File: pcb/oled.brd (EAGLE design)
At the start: 26.2 x 26.2 mm, 22 parts, among them U1 UG-2828GDEDF11, U3 FAN5331SX

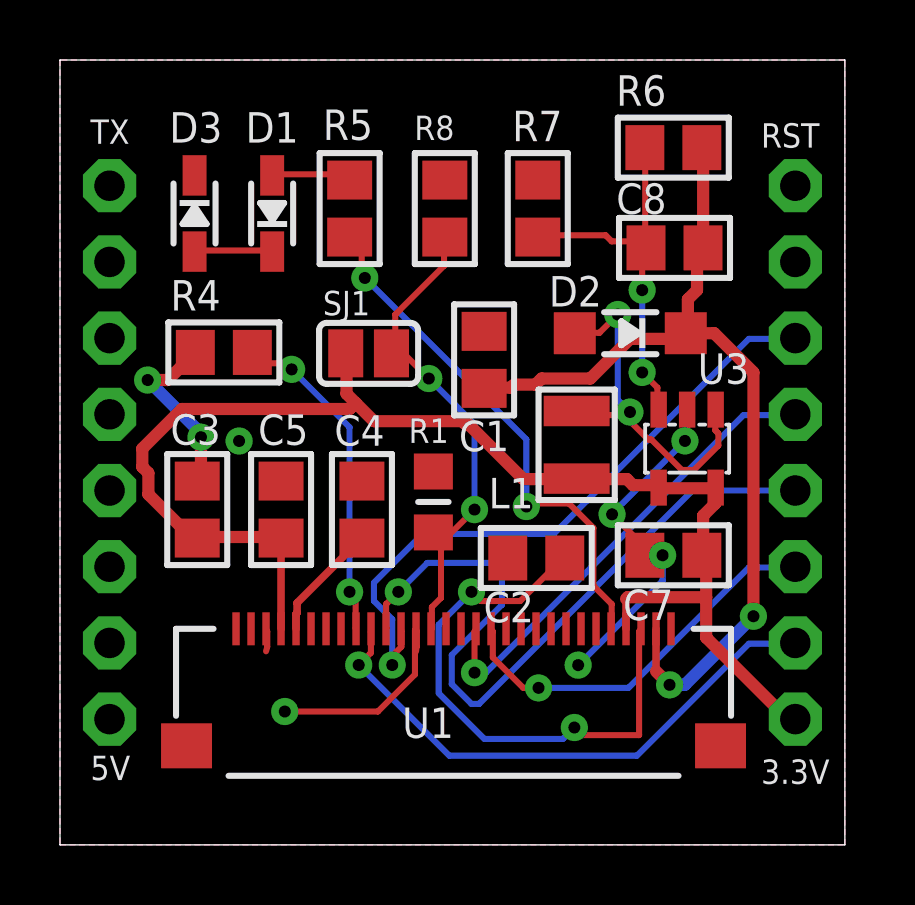
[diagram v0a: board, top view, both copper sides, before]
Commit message: USB board schematic V2 done
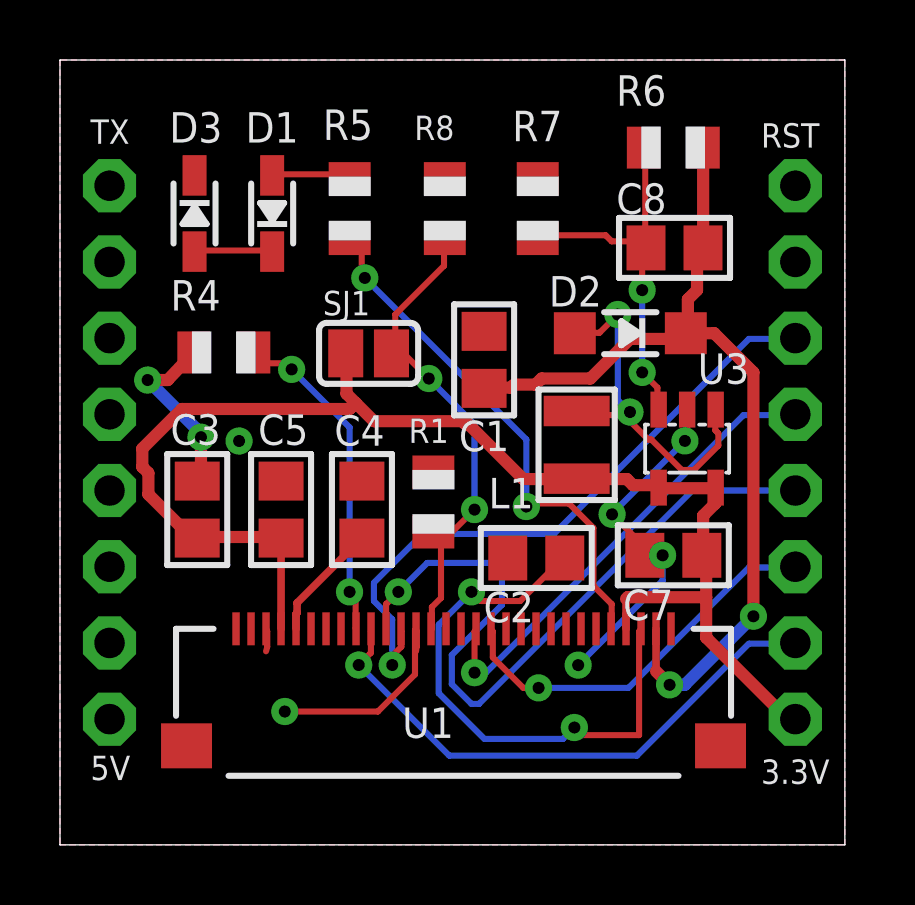
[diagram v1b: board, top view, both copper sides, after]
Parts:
- R1: device microbuilder:_0805MP -> adafruit:R0805
- R4, R5, R6, R7, R8: device microbuilder:0805 -> adafruit:R0805
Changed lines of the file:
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@@
 </autorouter>
 <elements>
-<element name="R4" library="microbuilder" package="0805" value="600K" x="5.461" y="16.414" smashed="yes">
+<element name="R4" library="adafruit" library_urn="urn:adsk.eagle:library:420" package="R0805" package3d_urn="urn:adsk.eagle:package:6240566/1" value="600K" x="5.461" y="16.414" smashed="yes">
 <attribute name="NAME" x="3.683" y="17.811" size="1.016" layer="25"/>
 <attribute name="VALUE" x="3.175" y="16.352" size="1.016" layer="27" rot="R180"/>
@@
 <attribute name="VALUE" x="4.194" y="8.763" size="1.016" layer="27" rot="R270"/>
 </element>
-<element name="R5" library="microbuilder" package="0805" value="50" x="9.655" y="21.209" smashed="yes" rot="R270">
+<element name="R5" library="adafruit" library_urn="urn:adsk.eagle:library:420" package="R0805" package3d_urn="urn:adsk.eagle:package:6240566/1" value="50" x="9.655" y="21.209" smashed="yes" rot="R270">
 <attribute name="NAME" x="8.763" y="23.498" size="1.016" layer="25"/>
 <attribute name="VALUE" x="9.274" y="17.907" size="1.016" layer="27" rot="R270"/>
@@
 <attribute name="NAME" x="16.296" y="17.944" size="1.016" layer="25"/>
 </element>
-<element name="R6" library="microbuilder" package="0805" value="100K" x="20.444" y="23.241" smashed="yes">
+<element name="R6" library="adafruit" library_urn="urn:adsk.eagle:library:420" package="R0805" package3d_urn="urn:adsk.eagle:package:6240566/1" value="100K" x="20.444" y="23.241" smashed="yes">
 <attribute name="NAME" x="18.539" y="24.638" size="1.016" layer="25"/>
 <attribute name="VALUE" x="18.793" y="21.209" size="1.016" layer="27"/>
 </element>
-<element name="R7" library="microbuilder" package="0805" value="10K" x="15.925" y="21.209" smashed="yes" rot="R270">
+<element name="R7" library="adafruit" library_urn="urn:adsk.eagle:library:420" package="R0805" package3d_urn="urn:adsk.eagle:package:6240566/1" value="10K" x="15.925" y="21.209" smashed="yes" rot="R270">
 <attribute name="NAME" x="15.076" y="23.455" size="1.016" layer="25"/>
 <attribute name="VALUE" x="17.693" y="19.775" size="1.016" layer="27" rot="R90"/>
@@
 <attribute name="NAME" x="3.646" y="23.408" size="1.016" layer="25"/>
 </element>
-<element name="R8" library="microbuilder" package="0805" value="10K" x="12.827" y="21.209" smashed="yes" rot="R270">
+<element name="R8" library="adafruit" library_urn="urn:adsk.eagle:library:420" package="R0805" package3d_urn="urn:adsk.eagle:package:6240566/1" value="10K" x="12.827" y="21.209" smashed="yes" rot="R270">
 <attribute name="NAME" x="11.811" y="23.495" size="0.8128" layer="25" ratio="18"/>
 <attribute name="VALUE" x="12.065" y="19.177" size="0.4064" layer="27" ratio="10" rot="R270"/>
@@
 <attribute name="VALUE" x="9.8869" y="16.383" size="0.02" layer="27" rot="R180"/>
 </element>
-<element name="R1" library="microbuilder" package="_0805MP" value="10K" x="12.446" y="11.43" smashed="yes" rot="R270">
+<element name="R1" library="adafruit" library_urn="urn:adsk.eagle:library:420" package="R0805" package3d_urn="urn:adsk.eagle:package:6240566/1" value="10K" x="12.446" y="11.43" smashed="yes" rot="R270">
 <attribute name="NAME" x="11.6205" y="13.3985" size="0.8128" layer="25" ratio="18"/>
 <attribute name="VALUE" x="11.176" y="13.0175" size="0.4064" layer="27" ratio="10" rot="R270"/>
@@
 <wire x1="12.7" y1="8.2296" x2="12.3952" y2="7.9248" width="0.2032" layer="1"/>
 <wire x1="12.7" y1="10.16" x2="12.7" y2="8.2296" width="0.2032" layer="1"/>
-<wire x1="12.446" y1="10.414" x2="12.7" y2="10.16" width="0.2032" layer="1"/>
+<wire x1="12.446" y1="10.43" x2="12.7" y2="10.16" width="0.2032" layer="1"/>
 <wire x1="12.3952" y1="7.2136" x2="12.368" y2="7.202" width="0.2032" layer="1"/>
 <wire x1="12.8016" y1="19.304" x2="12.8016" y2="20.2184" width="0.2032" layer="1"/>
@@
 <wire x1="11.176" y1="16.6624" x2="11.176" y2="17.6784" width="0.2032" layer="1"/>
 <wire x1="11.0744" y1="16.4592" x2="11.176" y2="16.5608" width="0.2032" layer="1"/>
-<wire x1="12.8016" y1="20.2184" x2="12.827" y2="20.259" width="0.2032" layer="1"/>
+<wire x1="12.8016" y1="20.2184" x2="12.827" y2="20.209" width="0.2032" layer="1"/>
 <wire x1="11.0744" y1="16.4592" x2="11.049" y2="16.383" width="0.2032" layer="1"/>
 <wire x1="12.9032" y1="10.2616" x2="12.7" y2="10.2616" width="0.2032" layer="1"/>
@@
 <wire x1="12.2936" y1="15.5448" x2="13.8176" y2="14.0208" width="0.2032" layer="16"/>
 <wire x1="11.176" y1="16.6624" x2="12.2936" y2="15.5448" width="0.2032" layer="1"/>
-<wire x1="12.7" y1="10.2616" x2="12.446" y2="10.414" width="0.2032" layer="1"/>
+<wire x1="12.7" y1="10.2616" x2="12.446" y2="10.43" width="0.2032" layer="1"/>
 <wire x1="11.176" y1="16.6624" x2="11.049" y2="16.383" width="0.2032" layer="1"/>
 <via x="13.8176" y="11.176" extent="1-16" drill="0.4"/>
@@
 <wire x1="11.8872" y1="7.112" x2="11.868" y2="7.202" width="0.2032" layer="1"/>
 <wire x1="11.8872" y1="6.604" x2="11.86798125" y2="6.452246875" width="0.2032" layer="1"/>
-<wire x1="4.511" y1="16.414" x2="3.591" y2="15.494" width="0.4064" layer="1"/>
+<wire x1="4.461" y1="16.414" x2="3.591" y2="15.494" width="0.4064" layer="1"/>
 <wire x1="3.591" y1="15.494" x2="2.921" y2="15.494" width="0.4064" layer="1"/>
 <via x="2.921" y="15.494" extent="1-16" drill="0.4"/>
@@
 <wire x1="20.0868" y1="8.806" x2="17.272" y2="5.9912" width="0.2032" layer="16"/>
 <via x="17.272" y="5.9912" extent="1-16" drill="0.4"/>
+<wire x1="12.827" y1="22.209" x2="15.925" y2="22.209" width="0" layer="19" extent="1-1"/>
+<wire x1="14.137" y1="17.116" x2="12.827" y2="22.209" width="0" layer="19" extent="1-1"/>
+<wire x1="12.446" y1="12.43" x2="14.137" y2="17.116" width="0" layer="19" extent="1-1"/>
+<wire x1="10.064" y1="12.126" x2="12.446" y2="12.43" width="0" layer="19" extent="1-1"/>
+<wire x1="7.369" y1="12.126" x2="10.064" y2="12.126" width="0" layer="19" extent="1-1"/>
+<wire x1="5.969" y1="13.462" x2="7.369" y2="12.126" width="0" layer="19" extent="1-1"/>
+<wire x1="4.699" y1="13.589" x2="5.969" y2="13.462" width="0" layer="19" extent="1-1"/>
+<wire x1="14.925" y1="9.562" x2="12.446" y2="12.43" width="0" layer="19" extent="1-1"/>
+<wire x1="18.4023" y1="11.01720625" x2="14.925" y2="9.562" width="0" layer="19" extent="1-1"/>
+<wire x1="20.368" y1="7.202" x2="20.0868" y2="9.652" width="0" layer="19" extent="1-1"/>
+<wire x1="11.868" y1="7.202" x2="14.925" y2="9.562" width="0" layer="19" extent="1-1"/>
+<wire x1="6.86798125" y1="6.45225" x2="7.493" y2="4.445" width="0" layer="19" extent="1-1"/>
+<wire x1="5.868" y1="7.202" x2="6.868" y2="7.202" width="0" layer="19" extent="1-1"/>
+<wire x1="1.651" y1="6.731" x2="5.868" y2="7.202" width="0" layer="19" extent="1-1"/>
+<wire x1="4.485" y1="22.315" x2="4.461" y2="16.414" width="0" layer="19" extent="1-1"/>
 </signal>
 <signal name="IREF">
@@
 <wire x1="6.5024" y1="16.3576" x2="6.8072" y2="16.0528" width="0.2032" layer="1"/>
 <wire x1="9.8552" y1="7.2136" x2="9.868" y2="7.202" width="0.2032" layer="1"/>
-<wire x1="6.5024" y1="16.3576" x2="6.411" y2="16.414" width="0.2032" layer="1"/>
+<wire x1="6.5024" y1="16.3576" x2="6.461" y2="16.414" width="0.2032" layer="1"/>
 <via x="9.652" y="8.4328" extent="1-16" drill="0.4"/>
 <via x="7.7216" y="15.8496" extent="1-16" drill="0.4"/>
@@
 <wire x1="9.7536" y1="20.2184" x2="10.0584" y2="19.9136" width="0.2032" layer="1"/>
 <wire x1="18.3896" y1="7.2136" x2="18.368" y2="7.202" width="0.2032" layer="1"/>
-<wire x1="9.7536" y1="20.2184" x2="9.655" y2="20.259" width="0.2032" layer="1"/>
+<wire x1="9.7536" y1="20.2184" x2="9.655" y2="20.209" width="0.2032" layer="1"/>
 <via x="15.5448" y="11.2776" extent="1-16" drill="0.4"/>
 <via x="10.16" y="18.8976" extent="1-16" drill="0.4"/>
@@
 <wire x1="9.652" y1="22.2504" x2="9.5504" y2="22.352" width="0.2032" layer="1"/>
 <wire x1="7.112" y1="22.352" x2="7.072" y2="22.315" width="0.2032" layer="1"/>
-<wire x1="9.652" y1="22.2504" x2="9.655" y2="22.159" width="0.2032" layer="1"/>
+<wire x1="9.652" y1="22.2504" x2="9.655" y2="22.209" width="0.2032" layer="1"/>
 </signal>
 <signal name="13V" class="1">
@@
 <wire x1="20.828" y1="16.8656" x2="20.86" y2="17.055" width="0.4064" layer="1"/>
 <wire x1="21.4376" y1="20.0152" x2="21.4376" y2="23.1648" width="0.4064" layer="1"/>
-<wire x1="21.4376" y1="23.1648" x2="21.394" y2="23.241" width="0.4064" layer="1"/>
+<wire x1="21.4376" y1="23.1648" x2="21.444" y2="23.241" width="0.4064" layer="1"/>
 <wire x1="21.4376" y1="20.0152" x2="21.434" y2="19.899" width="0.4064" layer="1"/>
 <wire x1="20.86" y1="17.055" x2="21.807" y2="17.055" width="0.4064" layer="1"/>
@@
 <wire x1="19.1008" y1="20.1168" x2="18.3896" y2="20.1168" width="0.2032" layer="1"/>
 <wire x1="19.4056" y1="19.812" x2="19.1008" y2="20.1168" width="0.2032" layer="1"/>
-<wire x1="15.9512" y1="20.32" x2="15.925" y2="20.259" width="0.2032" layer="1"/>
+<wire x1="15.9512" y1="20.32" x2="15.925" y2="20.209" width="0.2032" layer="1"/>
 <wire x1="19.4056" y1="19.812" x2="19.534" y2="19.899" width="0.2032" layer="1"/>
 <wire x1="19.5072" y1="19.9136" x2="19.5072" y2="23.1648" width="0.2032" layer="1"/>
-<wire x1="19.5072" y1="23.1648" x2="19.494" y2="23.241" width="0.2032" layer="1"/>
+<wire x1="19.5072" y1="23.1648" x2="19.444" y2="23.241" width="0.2032" layer="1"/>
 <wire x1="19.5072" y1="19.9136" x2="19.534" y2="19.899" width="0.2032" layer="1"/>
 <via x="19.4056" y="15.748" extent="1-16" drill="0.4"/>

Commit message: Rework Oled board to use VIN
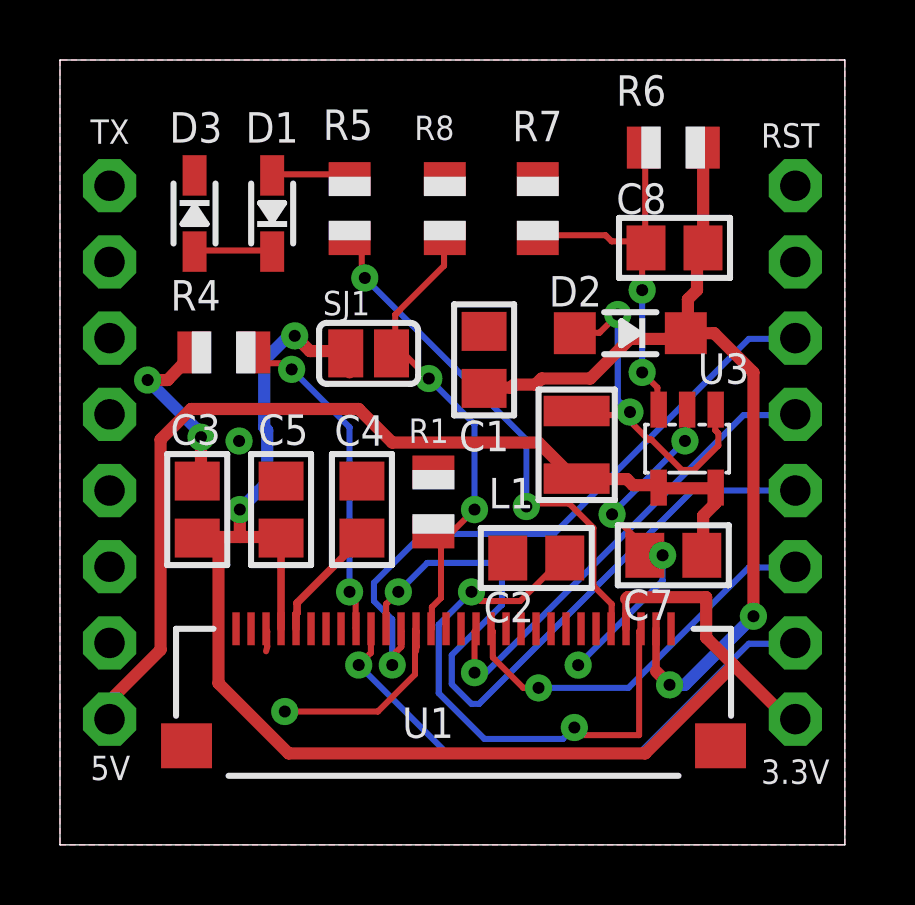
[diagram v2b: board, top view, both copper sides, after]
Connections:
- removed net 5V: JP2.8
- new net VIN: C7.1, JP2.8, L1.P$1, U3.4, U3.5
- net +3V3: no longer C7.1, L1.P$1, U3.4, U3.5
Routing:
- net VIN: track 0.00 -> 32.5 mm
- net +3V3: track 45.5 -> 50.4 mm, vias 0 -> 2

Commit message: V2 oled board ordered
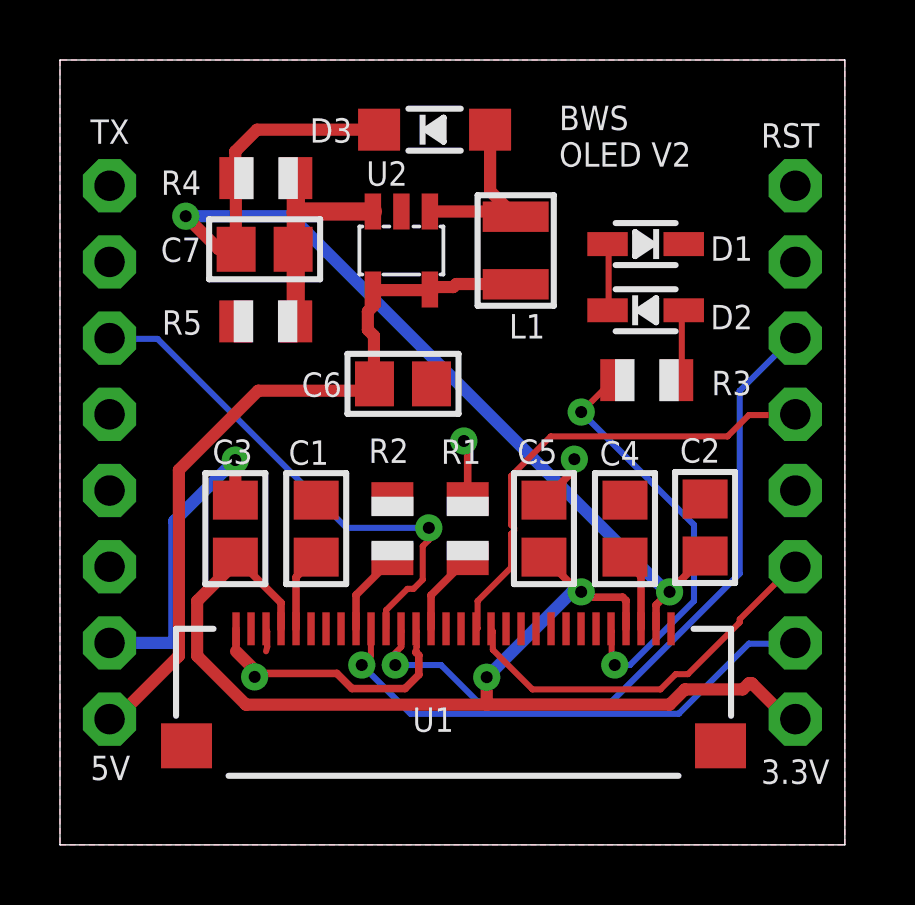
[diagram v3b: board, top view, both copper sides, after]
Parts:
- removed C8: 0.1uF, microbuilder:0805
- removed R6: 100K, adafruit:R0805
- removed R7, R8: 10K, adafruit:R0805
- removed SJ1: BS0, microbuilder:SOLDERJUMPER_REFLOW_NOPASTE
- removed U3: FAN5331SX, microbuilder:SOT23-5@1
- added C6: 10uF, microbuilder:0805
- added R2: 600K, adafruit:R0805
- added R3: 50, adafruit:R0805
- added U$1: (no value), Twitter:TWITTER5MM
- added U2: FAN5331SX, microbuilder:SOT23-5@1
- C1: value 10uF/16V -> 1.0uF
- C3: value 1.0uF -> 10uF
- C4: value 1.0uF -> 10uF/16V
- C5: value 10uF -> 1.0uF
- C7: value 10uF -> 0.1uF
- D2: value BAT54T1G -> 1N4148; device microbuilder:SOD-123 -> microbuilder:SOD-323
- D3: value 1N4148 -> BAT54T1G; device microbuilder:SOD-323 -> microbuilder:SOD-123
- R4: value 600K -> 100K
- R5: value 50 -> 10K
- moved JP1 22.9 mm to (1.65, 13.1), turned to 270 degrees
- moved JP2 22.9 mm to (24.5, 13.1), turned to 90 degrees
- moved C7 17.0 mm to (6.82, 19.9), turned to 0 degrees
- moved D1 12.5 mm to (19.5, 20.0), turned to 180 degrees
- moved C4 8.79 mm to (18.8, 10.5)
- moved C5 8.79 mm to (16.1, 10.5), turned to 270 degrees
- moved D3 8.47 mm to (12.5, 23.8), turned to 0 degrees
- moved C1 7.94 mm to (8.54, 10.5), turned to 90 degrees
- moved L1 6.79 mm to (15.2, 19.8)
- moved R4 5.98 mm to (6.86, 22.2), turned to 180 degrees
- moved C2 5.72 mm to (21.5, 10.6), turned to 270 degrees
- moved R5 4.69 mm to (6.86, 17.4), turned to 0 degrees
- moved R1 1.45 mm to (13.6, 10.5)
- moved C3 1.42 mm to (5.84, 10.5), turned to 90 degrees
- moved D2 0.92 mm to (19.5, 17.8), turned to 0 degrees
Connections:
- removed net D6/GPIO12: JP1.4, U1.P$11
- new net D6/GPIO12/MISO: JP2.4
- net +3V3: now also C3.1, C5.2, JP2.1; no longer C3.2, C5.1, JP1.1, SJ1.2
- net 13V: now also C2.2, C7.1, D3.C, R4.2; no longer C1.2, C8.1, D2.C, R6.2
- net A0: now also JP2.7; no longer JP1.7
- net D0/GPIO16: now also JP2.6; no longer JP1.6
- net D1/GPIO5: now also JP1.3, U1.P$11; no longer JP2.3
- net D2/GPIO4: now also JP1.4; no longer JP2.4
- net D3/GPIO0: now also JP1.5; no longer JP2.5
- net D4/GPIO2: now also JP1.6; no longer JP2.6
- net D5/GPIO14/SCK: now also JP2.5; no longer JP1.5
- net D7/GPIO13/MOSI: now also JP2.3; no longer JP1.3
- net D8/GPIO15: now also JP2.2; no longer JP1.2
- net GND: now also C1.2, C2.1, C3.2, C5.1, C6.2, D1.C, JP1.7, R2.1, R5.1, U2.2; no longer C1.1, C2.2, C3.1, C5.2, C7.2, D3.C, JP2.7, R4.1, R7.1, R8.1, U3.2
- net IREF: now also R2.2; no longer R4.2
- net N$11: now also D1.A, D2.C; no longer D1.C, D3.A
- net N$3: now also C1.1; no longer C4.1
- net N$5: now also D3.A, U2.1; no longer D2.A, U3.1
- net N$6: now also R3.2; no longer R5.2
- net N$7: now also D2.A, R3.1; no longer D1.A, R5.1
- net N$8: now also C7.2, R4.1, R5.2, U2.3; no longer C8.2, R6.1, R7.2, U3.3
- net OLED_BS0: no longer R8.2, SJ1.1
- net RESET: now also JP2.8; no longer JP1.8
- net RX: now also JP1.2; no longer JP2.2
- net TX: now also JP1.1; no longer JP2.1
- net VCOMH: now also C4.1; no longer C2.1
- net VIN: now also C6.1, JP1.8, U2.4, U2.5; no longer C7.1, JP2.8, U3.4, U3.5
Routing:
- net D6/GPIO12: track 24.5 -> 0.00 mm, vias 1 -> 0
- net D1/GPIO5: track 0.00 -> 17.3 mm, vias 0 -> 1
- net VCOMH: track 18.8 -> 2.61 mm, vias 2 -> 0
- net OLED_BS0: track 16.7 -> 2.84 mm, vias 2 -> 0
- net +3V3: track 50.4 -> 37.9 mm
- net IREF: track 11.0 -> 2.84 mm, vias 2 -> 0
- net VIN: track 32.5 -> 25.2 mm
- net N$8: track 13.0 -> 7.48 mm, vias 2 -> 0
- net N$5: track 12.4 -> 7.15 mm, vias 2 -> 0
- net 13V: track 30.7 -> 34.9 mm
- net N$6: track 17.7 -> 14.3 mm
- net D0/GPIO16: track 21.8 -> 23.9 mm
- net D8/GPIO15: track 18.7 -> 17.4 mm
- net N$3: track 3.93 -> 2.67 mm
- net GND: track 25.8 -> 24.8 mm, vias 8 -> 4
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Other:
- board text added: "BWS OLED V2"
- board text added: "D0(CS)"
- board text added: "D1(DC)"
- board text added: "D5(SCK)"
- board text added: "D7(MOSI)"
- board text added: "D8(RES)"
- board text added: "VIN"
- board text removed: "D0"
- board text removed: "D1"
- board text removed: "D5"
- board text removed: "D7"
- board text removed: "D8"
